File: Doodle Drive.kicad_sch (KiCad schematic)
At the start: 37 parts, among them J1 USB_B, J2 USB_B, J3 Screw_Terminal_01x02, J6 PINHD_1x2_Male, U1 STM32F411RETx, U6 AP7343-33W5-7, U7 CP2102-GMR, Y1 32.768KHz ±20ppm 12.5pF, Y2 25MHZ 12PF

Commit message: fixed variuopus stuff, this is probaly the bestellte version
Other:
- note added: "CKL"
- note added: "IO"
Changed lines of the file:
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@@
   (junction (at 86.36 51.435) (diameter 0) (color 0 0 0 0)
   )
+  (junction (at 257.81 134.62) (diameter 0) (color 0 0 0 0)
+  )
+  (junction (at 74.93 71.755) (diameter 0) (color 0 0 0 0)
+  )
   (junction (at 116.205 51.435) (diameter 0) (color 0 0 0 0)
-  )
-  (junction (at 257.81 134.62) (diameter 0) (color 0 0 0 0)
-  )
-  (junction (at 74.93 71.755) (diameter 0) (color 0 0 0 0)
   )
   (junction (at 170.815 67.31) (diameter 0) (color 0 0 0 0)
@@
     (stroke (width 0) (type default))
   )
+  (wire (pts (xy 116.205 43.815) (xy 116.205 51.435))
+    (stroke (width 0) (type default))
+  )
   (wire (pts (xy 236.22 134.62) (xy 257.81 134.62))
     (stroke (width 0) (type default))
@@
     (stroke (width 0) (type default))
   )
-  (wire (pts (xy 116.205 43.815) (xy 116.205 51.435))
-    (stroke (width 0) (type default))
-  )
   (wire (pts (xy 26.035 116.205) (xy 27.305 116.205))
     (stroke (width 0) (type default))
@@
   (polyline (pts (xy 100.965 24.13) (xy 100.965 69.215))
     (stroke (width 0) (type default))
+  )
+  (text "CKL" (at 197.485 31.115 0)
+    (effects (font (size 1.27 1.27)) (justify left bottom))
   )
   (text "Crystal configuration" (at 70.485 35.56 0)
     (effects (font (size 1.27 1.27)) (justify left bottom))
   )
+  (text "IO" (at 197.485 27.94 0)
+    (effects (font (size 1.27 1.27)) (justify left bottom))
+  )

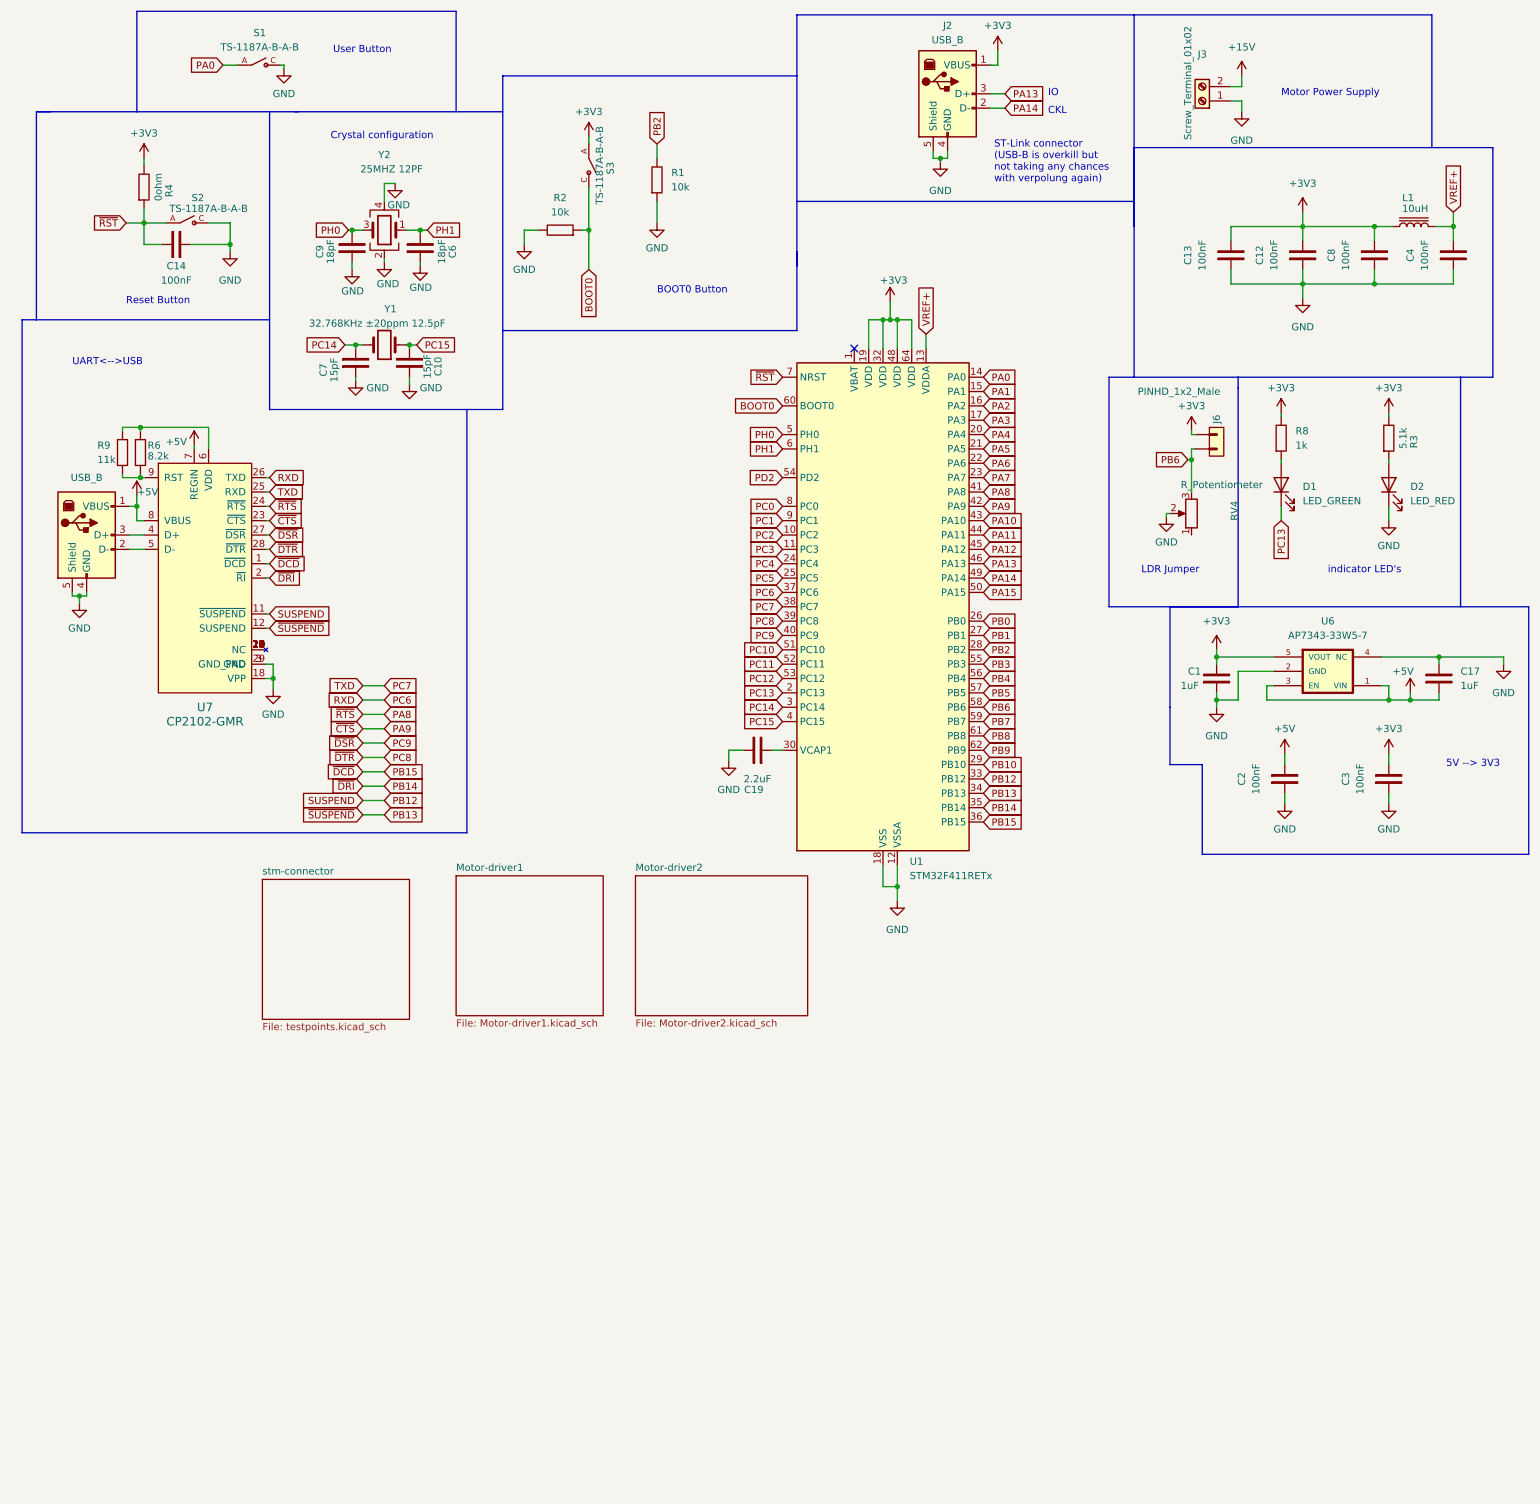
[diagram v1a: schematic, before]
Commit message: added pins for motor edge sensors, reroutet driver modules, removed module potentiometer, made everything more compact, fixed labels
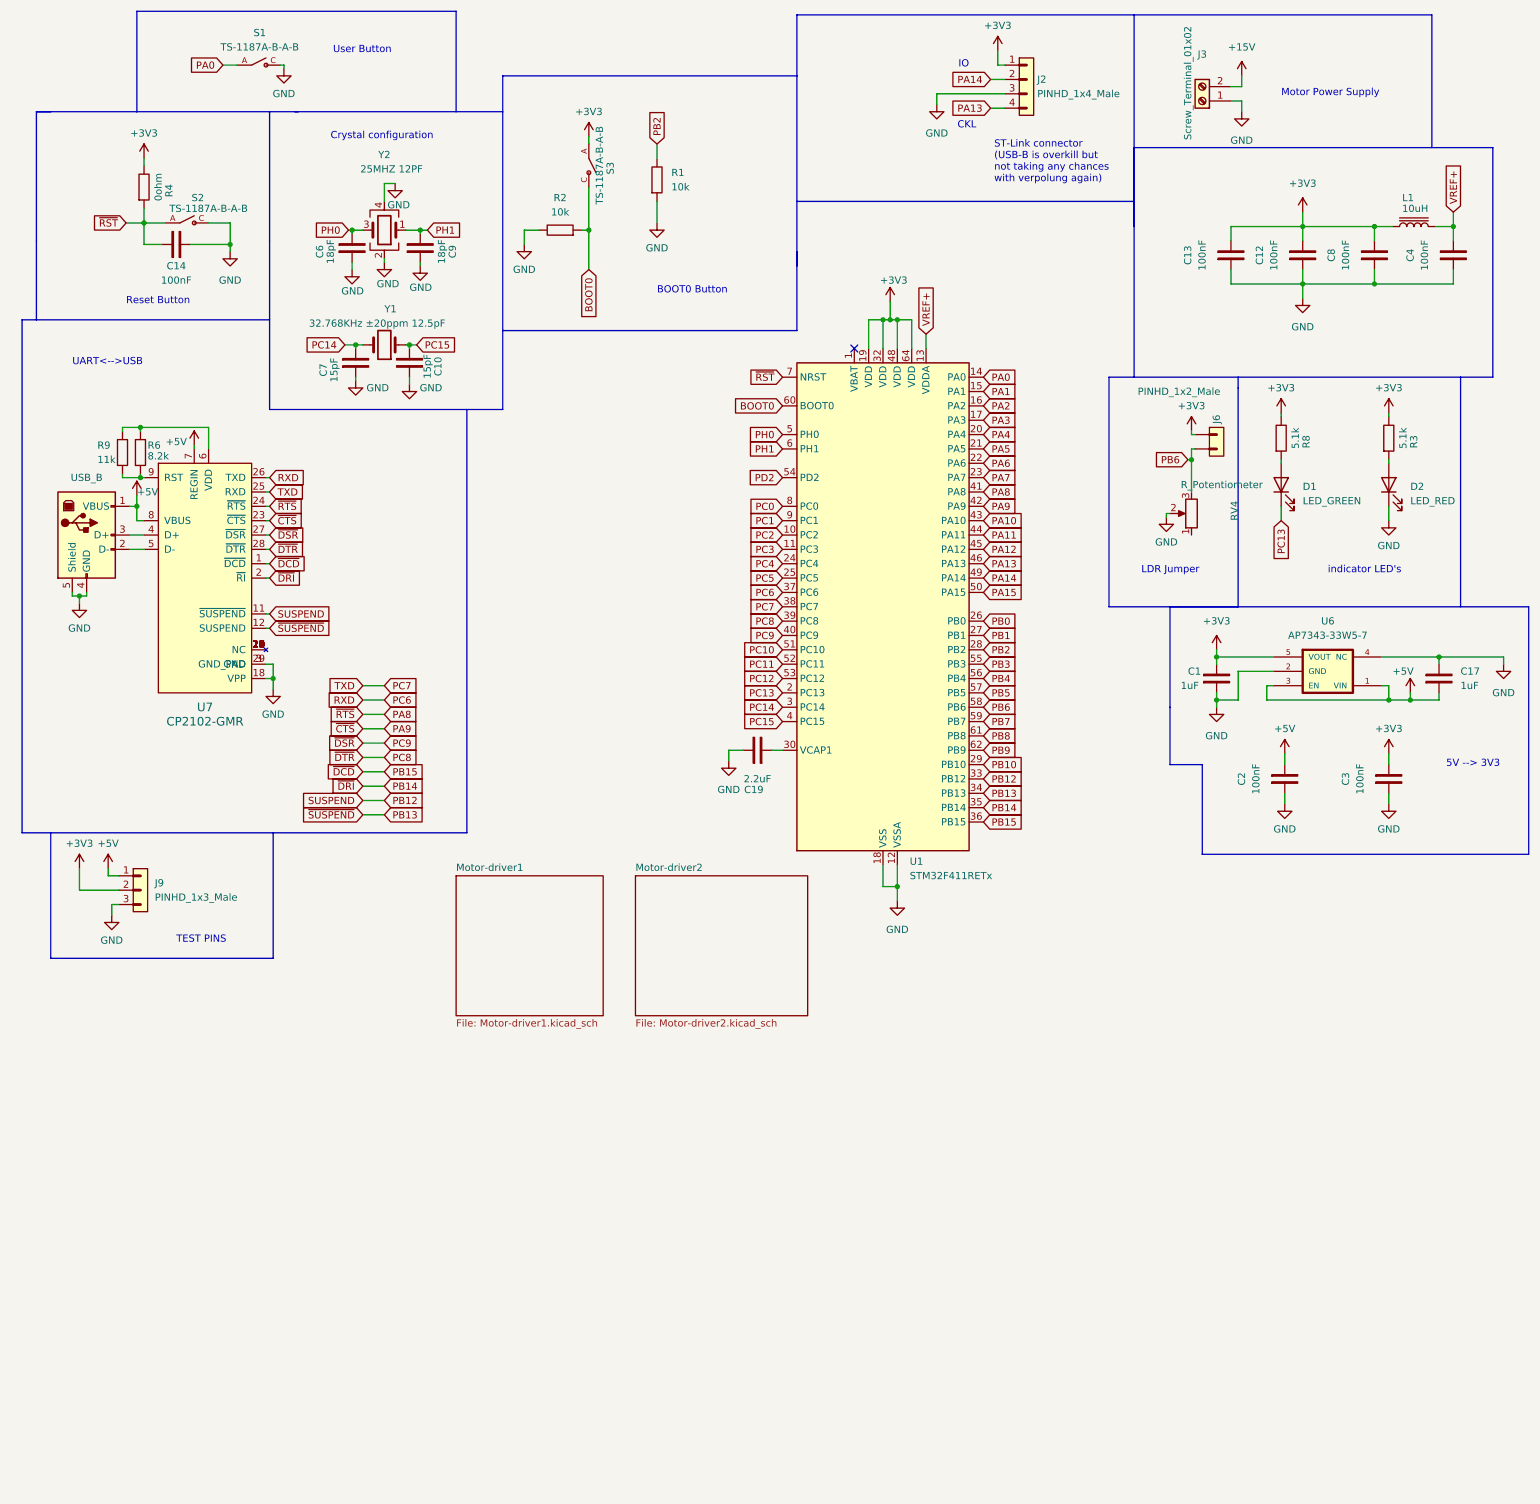
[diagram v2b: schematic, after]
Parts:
- removed J2: USB_B, Connector_USB:USB_B_Lumberg_2411_02_Horizontal, symbol Connector:USB_B
- added J2: PINHD_1x4_Male, Connector_PinHeader_2.54mm:PinHeader_1x04_P2.54mm_Vertical, symbol PCM_SL_Pin_Headers:PINHD_1x4_Male
- added J9: PINHD_1x3_Male, Connector_PinHeader_2.54mm:PinHeader_1x03_P2.54mm_Vertical, symbol PCM_SL_Pin_Headers:PINHD_1x3_Male
- C6, C9: footprint Capacitor_SMD:C_0805_2012Metric -> Capacitor_SMD:C_0402_1005Metric
- R8: value 1k -> 5.1k
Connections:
- net +3V3: now also J2.1, J9.2
- net +5V: now also J9.1
- net GND: now also J2.3, J9.3
- net PA13: now also J2.4
- net PA14: now also J2.2
- net PH0: now also C6.2; no longer C9.2
- net PH1: now also C9.2; no longer C6.2
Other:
- removed sheet stm-connector
- note added: "TEST PINS"

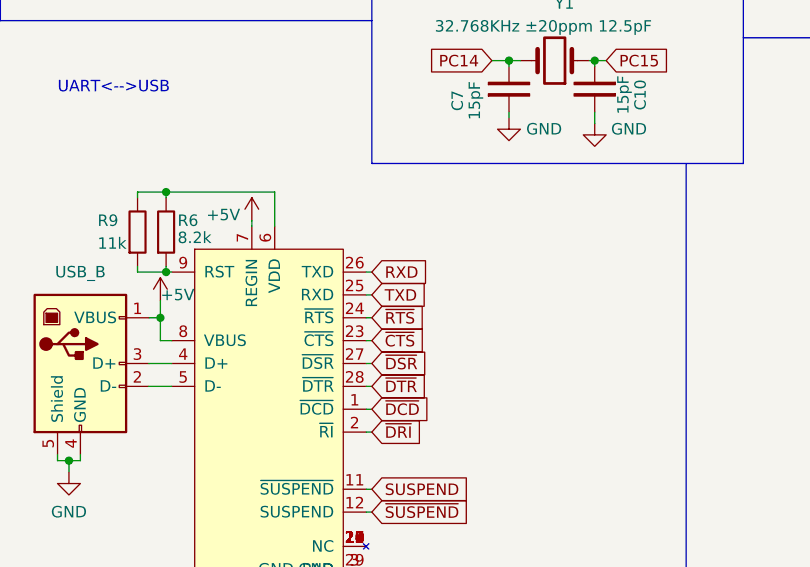
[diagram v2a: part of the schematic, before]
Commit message: fixed Serial connection, and various improvments
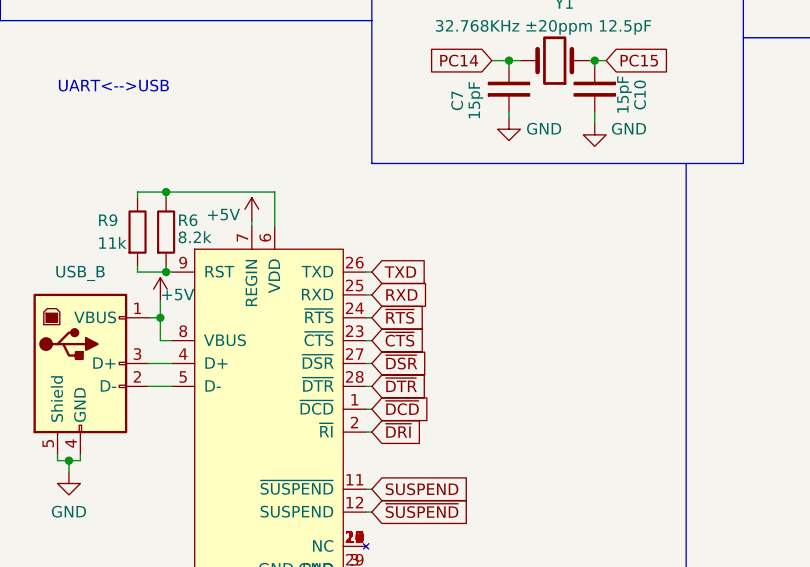
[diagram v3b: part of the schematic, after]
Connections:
- net PC6: now also U7.25 (RXD); no longer U7.26 (TXD)
- net PC7: now also U7.26 (TXD); no longer U7.25 (RXD)
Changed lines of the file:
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@@
-    )
-  )
-  (global_label "RXD" (shape input) (at 59.69 95.25 0) (fields_autoplaced)
-    (effects (font (size 1.27 1.27)) (justify left))
-    (property "Intersheetrefs" "${INTERSHEET_REFS}" (at 66.4247 95.25 0)
-      (effects (font (size 1.27 1.27)) (justify left) hide)
     )
   )
@@
     )
   )
+  (global_label "TXD" (shape input) (at 59.69 95.25 0) (fields_autoplaced)
+    (effects (font (size 1.27 1.27)) (justify left))
+    (property "Intersheetrefs" "${INTERSHEET_REFS}" (at 66.1223 95.25 0)
+      (effects (font (size 1.27 1.27)) (justify left) hide)
+    )
+  )
   (global_label "SUSPEND" (shape input) (at 76.2 152.4 180) (fields_autoplaced)
     (effects (font (size 1.27 1.27)) (justify right))
@@
     )
   )
+  (global_label "RXD" (shape input) (at 59.69 97.79 0) (fields_autoplaced)
+    (effects (font (size 1.27 1.27)) (justify left))
+    (property "Intersheetrefs" "${INTERSHEET_REFS}" (at 66.4247 97.79 0)
+      (effects (font (size 1.27 1.27)) (justify left) hide)
+    )
+  )
   (global_label "PB0" (shape input) (at 186.055 120.65 0) (fields_autoplaced)
     (effects (font (size 1.27 1.27)) (justify left))
@@
       (effects (font (size 1.27 1.27)) (justify left) hide)
     )
-  )
-  (global_label "TXD" (shape input) (at 59.69 97.79 0) (fields_autoplaced)
-    (effects (font (size 1.27 1.27)) (justify left))
-    (property "Intersheetrefs" "${INTERSHEET_REFS}" (at 66.1223 97.79 0)
-      (effects (font (size 1.27 1.27)) (justify left) hide)
-    )

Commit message: letzter code
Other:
- sheet Motor-driver1 renamed Motor-driver
- removed sheet Motor-driver2
- sheet Motor-driver: file Motor-driver1.kicad_sch -> Motor-driver.kicad_sch
- moved on the sheet: C1, C12, C13, C17, C19, C2, C3, C4, C8, D1, D2, J2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
